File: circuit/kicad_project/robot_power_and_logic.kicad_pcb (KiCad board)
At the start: 2 copper layers, 0 parts

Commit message: Create PCB elements layout
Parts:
- added C1: 330 nF, Capacitor_THT:C_Disc_D4.7mm_W2.5mm_P5.00mm, F.Cu at (87.6, 110.5)
- added C2: 100 nF, Capacitor_THT:C_Disc_D4.7mm_W2.5mm_P5.00mm, F.Cu at (76.2, 116.8)
- added C3: 100 nF, Capacitor_THT:C_Disc_D4.7mm_W2.5mm_P5.00mm, F.Cu at (76.2, 71.1)
- added C4: 1 µF, Capacitor_THT:C_Disc_D4.7mm_W2.5mm_P5.00mm, F.Cu at (94.0, 93.9)
- added H1: MountingHole, MountingHole:MountingHole_3.2mm_M3, F.Cu at (101.6, 115.6)
- added H2: MountingHole, MountingHole:MountingHole_3.2mm_M3, F.Cu at (101.6, 69.8)
- added H3: MountingHole, MountingHole:MountingHole_3.2mm_M3, F.Cu at (45.7, 69.8)
- added H4: MountingHole, MountingHole:MountingHole_3.2mm_M3, F.Cu at (45.7, 115.6)
- added J1: HC-05 connection socket, Connector_PinHeader_2.54mm:PinHeader_1x04_P2.54mm_Vertical, F.Cu at (48.3, 83.8)
- added J2: Power terminal, TerminalBlock_Phoenix:TerminalBlock_Phoenix_MPT-0,5-2-2.54_1x02_P2.54mm_Horizontal, F.Cu at (92.7, 115.6)
- added J3: right_track_motor+, Connector_PinSocket_2.54mm:PinSocket_1x01_P2.54mm_Vertical, F.Cu at (88.9, 74.9)
- added J4: right_track_motor-, Connector_PinSocket_2.54mm:PinSocket_1x01_P2.54mm_Vertical, F.Cu at (81.3, 74.9)
- added J5: left_track_motor+, Connector_PinSocket_2.54mm:PinSocket_1x01_P2.54mm_Vertical, F.Cu at (81.3, 90.2)
- added J6: left_track_motor-, Connector_PinSocket_2.54mm:PinSocket_1x01_P2.54mm_Vertical, F.Cu at (88.9, 90.2)
- added SW2: Reset, Button_Switch_THT:SW_PUSH_6mm_H4.3mm, F.Cu at (95.2, 105.9)
- added U1: LM7805_TO220, Package_TO_SOT_THT:TO-220-3_Vertical, F.Cu at (81.3, 110.5)
- added U2: Pico, MCU_RaspberryPi_and_Boards:RPi_Pico_SMD_TH, B.Cu at (62.2, 92.7)
- added U3: L293D, Package_DIP:DIP-16_W7.62mm, F.Cu at (76.2, 86.3)
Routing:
- added copper zone on F.Cu, net /GND
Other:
- board outline added: 63 x 53 mm

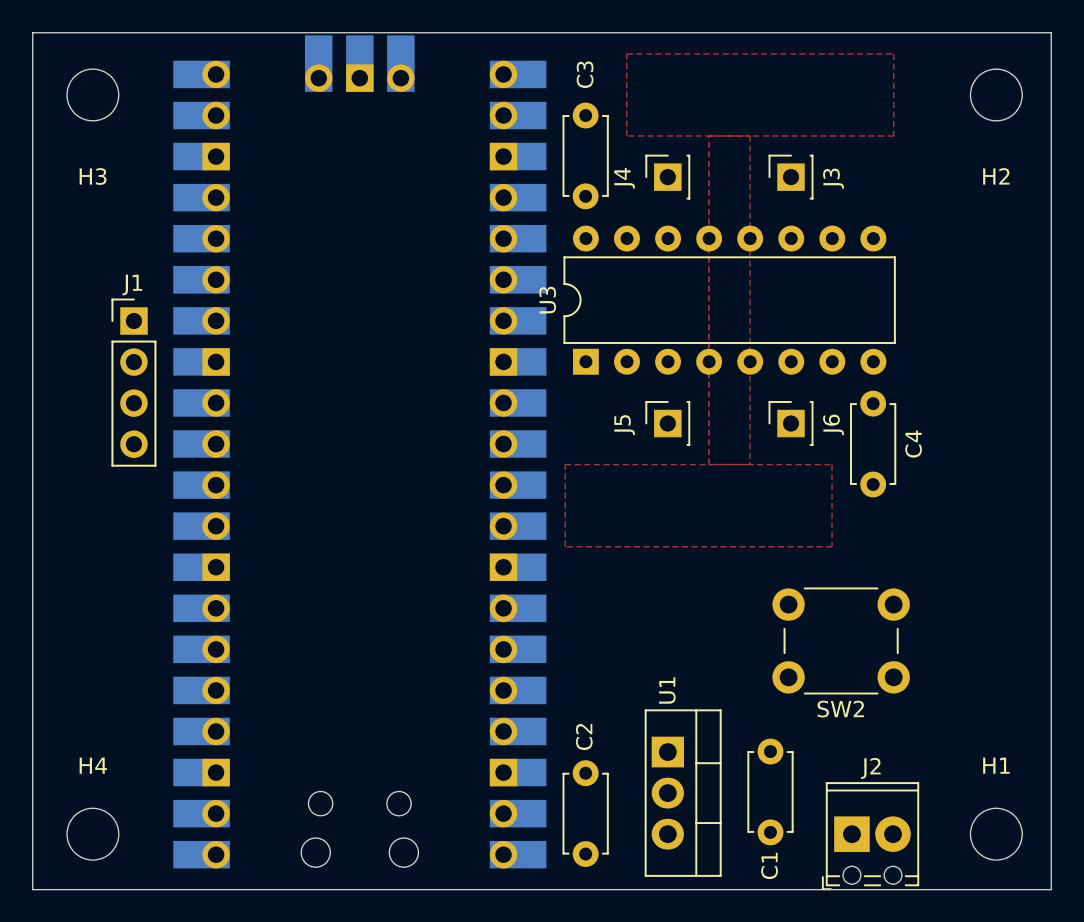
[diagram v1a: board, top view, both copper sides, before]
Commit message: Add routes to PCB design
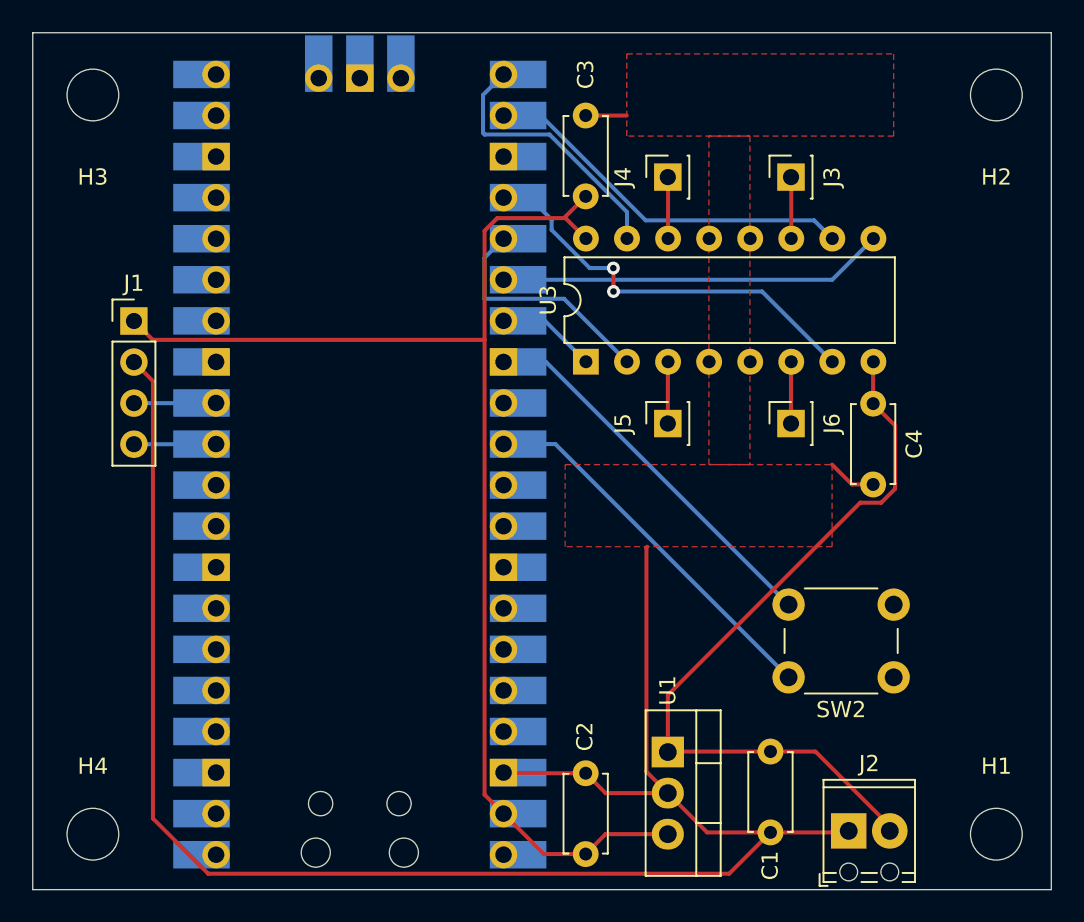
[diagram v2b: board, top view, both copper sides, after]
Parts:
- moved J2 0.29 mm to (92.5, 115.4)
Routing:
- net /GND: track 0.00 -> 113.7 mm
- net /+5V: track 0.00 -> 79.4 mm
- net /+7.4V: track 0.00 -> 47.3 mm
- net /left_track_motor_ch_in_2: track 0.00 -> 25.8 mm, vias 0 -> 2
- net /right_track_motor_en: track 0.00 -> 23.9 mm
- net Net-(SW2-Pad2): track 0.00 -> 23.8 mm
- net Net-(SW2-Pad1): track 0.00 -> 23.6 mm
- net /right_track_motor_ch_in_1: track 0.00 -> 23.5 mm
- net /right_track_motor_ch_in_2: track 0.00 -> 16.7 mm
- net /left_track_motor_ch_in_1: track 0.00 -> 14.6 mm
- net /left_track_motor_en: track 0.00 -> 6.14 mm
- net /HC-05 RX: track 0.00 -> 5.08 mm
- net /HC-05 TX: track 0.00 -> 5.08 mm
- net Net-(J6-Pad1): track 0.00 -> 3.83 mm
- net Net-(J5-Pad1): track 0.00 -> 3.83 mm
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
